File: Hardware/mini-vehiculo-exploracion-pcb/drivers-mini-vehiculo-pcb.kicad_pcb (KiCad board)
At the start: 2 copper layers, 75.5 x 100 mm, 56 parts, among them IC1 MAX8891EXK33_V+T, J1 Conn_01x08_Pin_drv, J2 Conn_01x02_Pin_drv, J4 Motor1_Terminal, J5 Motor2_Terminal, J6 Battery_Terminal_01x02, U1 DRV8873HPWPRQ1, U2 DRV8873HPWPRQ1, U3 TPS561208DDCR, U4 LM358

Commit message: cambios rama de drivers
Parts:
- L1: value 4,7u -> MLP2520S4R7MT0S1
- moved L1 1.00 mm to (74.0, 116.5)
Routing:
- net +5V: track 16.4 -> 21.9 mm
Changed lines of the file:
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@@
 		)
 	)
-	(footprint "MLP2520S4R7MT0S1:INDC2520X100N"
-		(layer "F.Cu")
-		(at 73.9 115.5)
-		(descr "MLP2520")
-		(tags "Inductor")
-		(property "Reference" "L1"
-			(at -0.06 2.28 0)
-			(layer "F.SilkS")
-			(effects
-				(font
-					(size 1.27 1.27)
-					(thickness 0.254)
-				)
-			)
-		)
-		(property "Value" "4,7u"
-			(at 0 0 0)
-			(layer "F.SilkS")
-			(hide yes)
-			(effects
-				(font
-					(size 1.27 1.27)
-					(thickness 0.254)
-				)
-			)
-		)
-		(property "Datasheet" "~"
-			(at 0 0 0)
-			(layer "F.Fab")
-			(hide yes)
-			(effects
-				(font
-					(size 1.27 1.27)
-					(thickness 0.15)
-				)
-			)
-		)
-		(property "Description" "Inductor"
-			(at 0 0 0)
-			(layer "F.Fab")
-			(hide yes)
-			(effects
-				(font
-					(size 1.27 1.27)
-					(thickness 0.15)
-				)
-			)
-		)
-		(property ki_fp_filters "Choke_* *Coil* Inductor_* L_*")
-		(sheetname "/Electrical/")
-		(sheetfile "electrical_drivers.kicad_sch")
-		(attr smd)
-		(fp_line
-			(start 0 -0.9)
-			(end 0 0.9)
-			(stroke
-				(width 0.2)
-				(type solid)
-			)
-			(layer "F.SilkS")
-		)
-		(fp_line
-			(start -1.925 -1.35)
-			(end 1.925 -1.35)
-			(stroke
-				(width 0.05)
-				(type solid)
-			)
-			(layer "F.CrtYd")
-		)
-		(fp_line
-			(start -1.925 1.35)
-			(end -1.925 -1.35)
-			(stroke
-				(width 0.05)
-				(type solid)
-			)
-			(layer "F.CrtYd")
-		)
-		(fp_line
-			(start 1.925 -1.35)
-			(end 1.925 1.35)
-			(stroke
-				(width 0.05)
-				(type solid)
-			)
-			(layer "F.CrtYd")
-		)
-		(fp_line
-			(start 1.925 1.35)
-			(end -1.925 1.35)
-			(stroke
-				(width 0.05)
-				(type solid)
-			)
-			(layer "F.CrtYd")
-		)
-		(fp_line
-			(start -1.25 -1)
-			(end 1.25 -1)
-			(stroke
-				(width 0.1)
-				(type solid)
-			)
-			(layer "F.Fab")
-		)
-		(fp_line
-			(start -1.25 1)
-			(end -1.25 -1)
-			(stroke
-				(width 0.1)
-				(type solid)
-			)
-			(layer "F.Fab")
-		)
-		(fp_line
-			(start 1.25 -1)
-			(end 1.25 1)
-			(stroke
-				(width 0.1)
-				(type solid)
-			)
-			(layer "F.Fab")
-		)
-		(fp_line
-			(start 1.25 1)
-			(end -1.25 1)
-			(stroke
-				(width 0.1)
-				(type solid)
-			)
-			(layer "F.Fab")
-		)
-		(pad "1" smd rect
-			(at -1.1 0)
-			(size 1.15 2.2)
-			(layers "F.Cu" "F.Mask" "F.Paste")
-			(net 25 "Net-(U3-SW)")
-			(pinfunction "1")
-			(pintype "passive")
-		)
-		(pad "2" smd rect
-			(at 1.1 0)
-			(size 1.15 2.2)
-			(layers "F.Cu" "F.Mask" "F.Paste")
-			(net 5 "+5V")
-			(pinfunction "2")
-			(pintype "passive")
-		)
-		(embedded_fonts no)
-		(model "MLP2520S4R7MT0S1.stp"
-			(offset
-				(xyz 0 0 0)
-			)
-			(scale
-				(xyz 1 1 1)
-			)
-			(rotate
-				(xyz 0 0 0)
-			)
-		)
-	)
 	(footprint "Capacitor_SMD:C_0805_2012Metric_Pad1.18x1.45mm_HandSolder"
 		(layer "F.Cu")
@@
 		)
 	)
+	(footprint "MLP2520S4R7MT0S1:INDC2520X100N"
+		(layer "F.Cu")
+		(at 74 116.5)
+		(descr "MLP2520")
+		(tags "Inductor")
+		(property "Reference" "L1"
+			(at 0 0 0)
+			(layer "F.SilkS")
+			(effects
+				(font
+					(size 1.27 1.27)
+					(thickness 0.254)
+				)
+			)
+		)
+		(property "Value" "MLP2520S4R7MT0S1"
+			(at 0 0 0)
+			(layer "F.SilkS")
+			(hide yes)
+			(effects
+				(font
+					(size 1.27 1.27)
+					(thickness 0.254)
+				)
+			)
+		)
+		(property "Datasheet" "https://product.tdk.com/system/files/dam/doc/product/inductor/inductor/smd/catalog/inductor_commercial_power_mlp2520_en.pdf"
+			(at 0 0 0)
+			(layer "F.Fab")
+			(hide yes)
+			(effects
+				(font
+					(size 1.27 1.27)
+					(thickness 0.15)
+				)
+			)
+		)
+		(property "Description" "Inductor Power Shielded Multi-Layer 4.7uH 20% 2MHz Ferrite 1A 169mOhm DCR 1008 T/R"
+			(at 0 0 0)
+			(layer "F.Fab")
+			(hide yes)
+			(effects
+				(font
+					(size 1.27 1.27)
+					(thickness 0.15)
+				)
+			)
+		)
+		(property "Height" "1"
+			(at 0 0 0)
+			(unlocked yes)
+			(layer "F.Fab")
+			(hide yes)
+			(effects
+				(font
+					(size 1 1)
+					(thickness 0.15)
+				)
+			)
+		)
+		(property "Mouser Part Number" "810-MLP2520S4R7MT0S1"
+			(at 0 0 0)
+			(unlocked yes)
+			(layer "F.Fab")
+			(hide yes)
+			(effects
+				(font
+					(size 1 1)
+					(thickness 0.15)
+				)
+			)
+		)
+		(property "Mouser Price/Stock" "https://www.mouser.co.uk/ProductDetail/TDK/MLP2520S4R7MT0S1?qs=%2FPzWLGNeQ%252BgDk3obJem54g%3D%3D"
+			(at 0 0 0)
+			(unlocked yes)
+			(layer "F.Fab")
+			(hide yes)
+			(effects
+				(font
+					(size 1 1)
+					(thickness 0.15)
+				)
+			)
+		)
+		(property "Manufacturer_Name" "TDK"
+			(at 0 0 0)
+			(unlocked yes)
+			(layer "F.Fab")
+			(hide yes)
+			(effects
+				(font
+					(size 1 1)
+					(thickness 0.15)
+				)
+			)
+		)
+		(property "Manufacturer_Part_Number" "MLP2520S4R7MT0S1"
+			(at 0 0 0)
+			(unlocked yes)
+			(layer "F.Fab")
+			(hide yes)
+			(effects
+				(font
+					(size 1 1)
+					(thickness 0.15)
+				)
+			)
+		)
+		(sheetname "/Electrical/")
+		(sheetfile "electrical_drivers.kicad_sch")
+		(attr smd)
+		(fp_line
+			(start 0 -0.9)
+			(end 0 0.9)
+			(stroke
+				(width 0.2)
+				(type solid)
+			)
+			(layer "F.SilkS")
+		)
+		(fp_line
+			(start -1.925 -1.35)
+			(end 1.925 -1.35)
+			(stroke
+				(width 0.05)
+				(type solid)
+			)
+			(layer "F.CrtYd")
+		)
+		(fp_line
+			(start -1.925 1.35)
+			(end -1.925 -1.35)
+			(stroke
+				(width 0.05)
+				(type solid)
+			)
+			(layer "F.CrtYd")
+		)
+		(fp_line
+			(start 1.925 -1.35)
+			(end 1.925 1.35)
+			(stroke
+				(width 0.05)
+				(type solid)
+			)
+			(layer "F.CrtYd")
+		)
+		(fp_line
+			(start 1.925 1.35)
+			(end -1.925 1.35)
+			(stroke
+				(width 0.05)
+				(type solid)
+			)
+			(layer "F.CrtYd")
+		)
+		(fp_line
+			(start -1.25 -1)
+			(end 1.25 -1)
+			(stroke
+				(width 0.1)
+				(type solid)
+			)
+			(layer "F.Fab")
+		)
+		(fp_line
+			(start -1.25 1)
+			(end -1.25 -1)
+			(stroke
+				(width 0.1)
+				(type solid)
+			)
+			(layer "F.Fab")
+		)
+		(fp_line
+			(start 1.25 -1)
+			(end 1.25 1)
+			(stroke
+				(width 0.1)
+				(type solid)
+			)
+			(layer "F.Fab")
+		)
+		(fp_line
+			(start 1.25 1)
+			(end -1.25 1)
+			(stroke
+				(width 0.1)
+				(type solid)
+			)
+			(layer "F.Fab")
+		)
+		(fp_text user "${REFERENCE}"
+			(at 0 0 0)
+			(layer "F.Fab")
+			(effects
+				(font
+					(size 1.27 1.27)
+					(thickness 0.254)
+				)
+			)
+		)
+		(pad "1" smd rect
+			(at -1.1 0)
+			(size 1.15 2.2)
+			(layers "F.Cu" "F.Mask" "F.Paste")
+			(net 25 "Net-(U3-SW)")
+			(pinfunction "1")
+			(pintype "passive")
+		)
+		(pad "2" smd rect
+			(at 1.1 0)
+			(size 1.15 2.2)
+			(layers "F.Cu" "F.Mask" "F.Paste")
+			(net 5 "+5V")
+			(pinfunction "2")
+			(pintype "passive")
+		)
+		(embedded_fonts no)
+		(model "MLP2520S4R7MT0S1.stp"
+			(offset
+				(xyz 0 0 0)
+			)
+			(scale
+				(xyz 1 1 1)
+			)
+			(rotate
+				(xyz 0 0 0)
+			)
+		)
+	)
 	(footprint "LM358AN_NOPB:DIP794W53P254L959H508Q8N"
 		(layer "F.Cu")
@@
 		(start 69.415 102.125)
 		(end 62.99 102.125)
-		(width 0.4)
+		(width 1.2)
 		(layer "F.Cu")
 		(net 2)
@@
 		(start 53.885 101.04)
 		(end 60.305 101.04)
-		(width 0.4)
+		(width 1.2)
 		(layer "F.Cu")
 		(net 2)
@@
 		(start 62.99 102.125)
 		(end 62.09 101.225)
-		(width 0.4)
+		(width 1.2)
 		(layer "F.Cu")
 		(net 2)
@@
 		(start 62.09 101.225)
 		(end 60.49 101.225)
-		(width 0.4)
+		(width 1.2)
 		(layer "F.Cu")
 		(net 2)
@@
 		(layer "F.Cu")
 		(net 5)
+	)
+	(segment
+		(start 76.949 116.5)
+		(end 79.499 119.05)
+		(width 0.4)
+		(layer "F.Cu")
+		(net 5)
+	)
+	(segment
+		(start 75.1 116.5)
+		(end 76.949 116.5)
+		(width 0.4)
+		(layer "F.Cu")
+		(net 5)

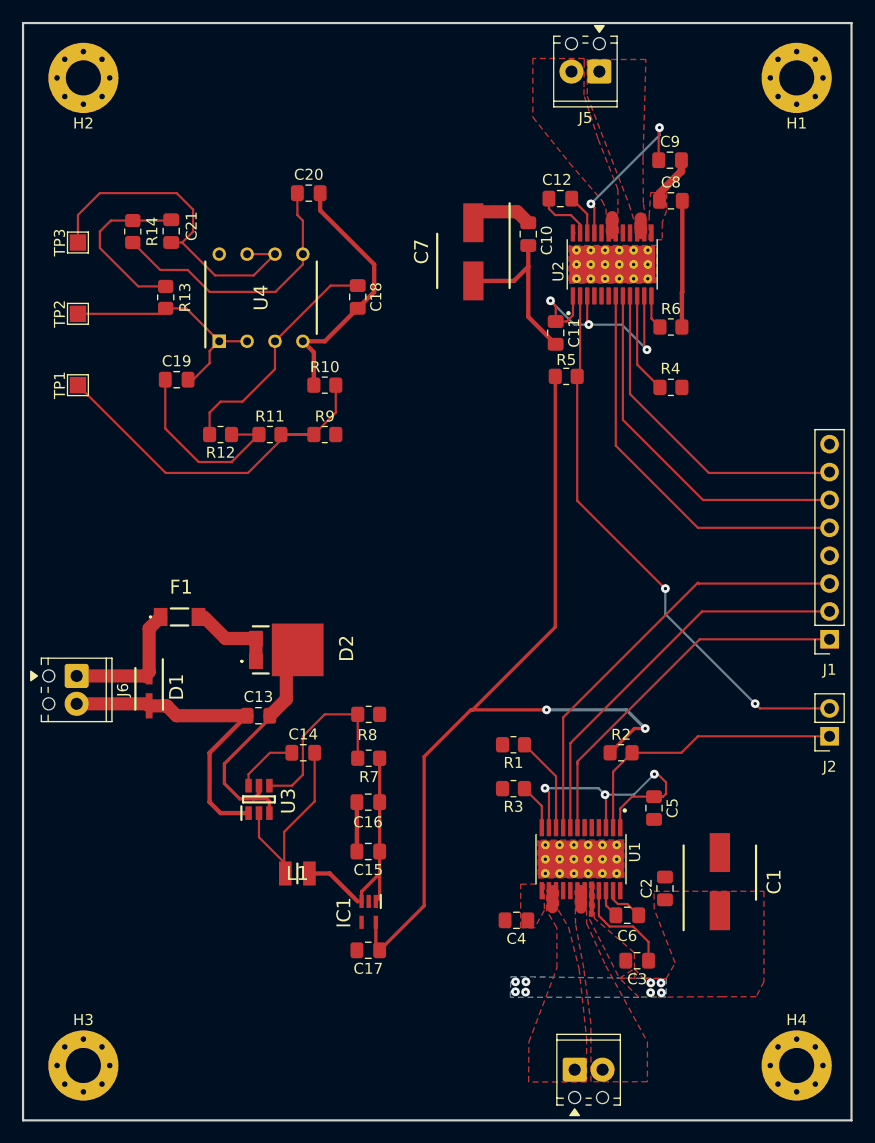
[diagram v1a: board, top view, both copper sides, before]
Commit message: updated gnd and 12v zones
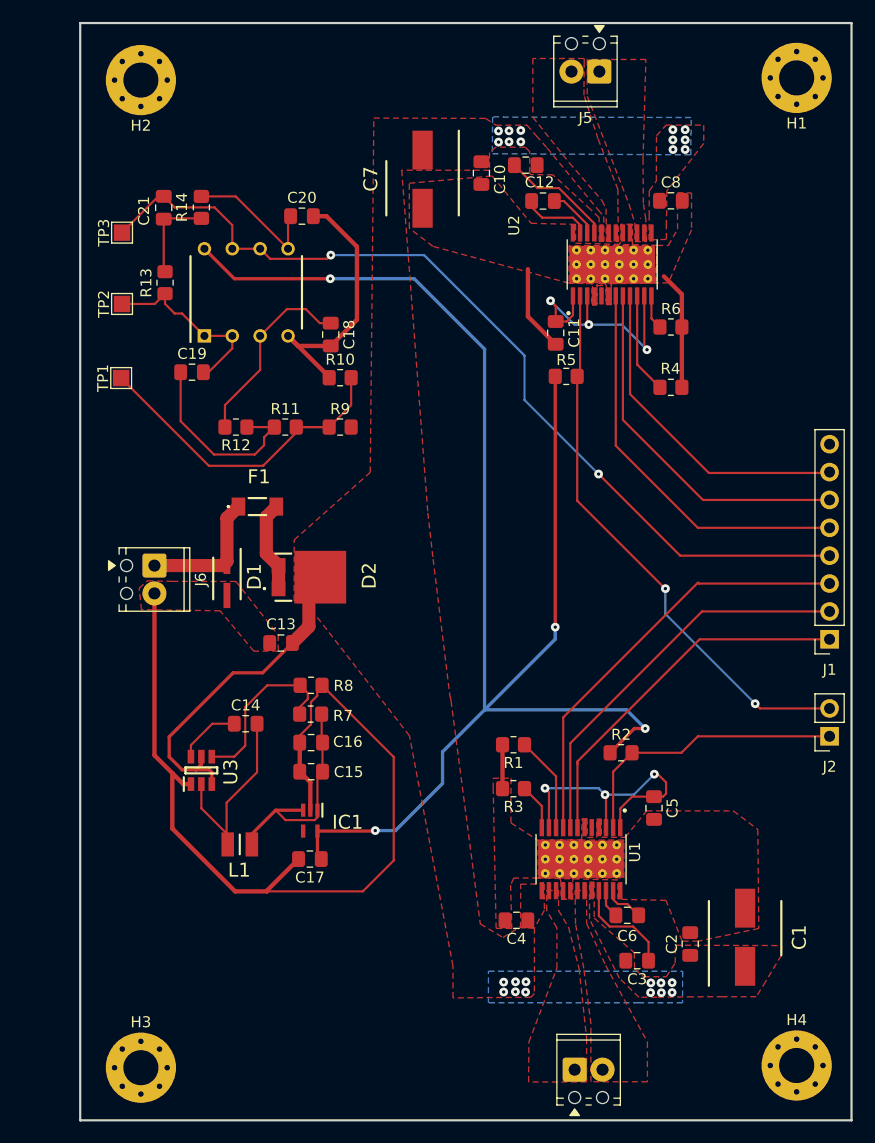
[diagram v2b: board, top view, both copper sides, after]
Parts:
- moved C9 13.2 mm to (94.8, 52.0)
- moved F1 12.3 mm to (70.4, 83.1)
- moved J6 12.3 mm to (61.0, 88.4)
- moved D1 12.3 mm to (67.6, 89.6)
- moved C17 9.87 mm to (75.1, 115.2)
- moved IC1 9.87 mm to (75.2, 111.7)
- moved C15 8.95 mm to (75.3, 107.2)
- moved C7 8.08 mm to (85.4, 53.2)
- moved C16 7.52 mm to (75.3, 104.6)
- moved C10 7.01 mm to (90.8, 52.7)
- moved C13 6.94 mm to (72.5, 95.5)
- moved D2 6.94 mm to (75.0, 89.5)
- moved R7 6.65 mm to (75.2, 102.0)
- moved R14 6.63 mm to (65.2, 55.8), turned to 90 degrees
- moved C14 5.88 mm to (69.3, 102.9)
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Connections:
- J1 pad 4: unconnected-(J1-Pin_4-Pad4) -> ADC_BAT
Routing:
- net +3.3V: track 82.4 -> 138.9 mm, vias 2 -> 4
- net ADC_BAT: track 32.3 -> 83.7 mm, vias 0 -> 2
- net GND: track 84.7 -> 130.9 mm
- net Net-(U4B-+): track 25.1 -> 12.9 mm
- net Net-(C21-Pad1): track 15.9 -> 8.40 mm
- net /VCP2: track 15.3 -> 10.4 mm, vias 2 -> 0
- net /Battery Sensor/OP1_OUT: track 21.8 -> 17.3 mm
- net Net-(U4A-+): track 21.8 -> 17.6 mm
- net +12V: track 34.8 -> 30.8 mm, vias 8 -> 24
- net Net-(R10-Pad2): track 34.6 -> 32.1 mm
- net /M1_V+: track 2.23 -> 0.00 mm
- net /M1_V-: track 2.29 -> 0.11 mm
- net /M2_V+: track 2.13 -> 0.03 mm
- net /M2_V-: track 2.24 -> 0.26 mm
- net +5V: track 21.9 -> 20.6 mm
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- added copper zone on B.Cu, net GND
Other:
- board size 75.5 x 100 mm -> 70.3 x 100 mm

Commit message: updated gnd plane
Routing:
- net GND: track 130.9 -> 1.36 mm

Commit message: updated driver pcb
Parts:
- moved J1 1.38 mm to (121.1, 95.2)
- moved J2 1.38 mm to (121.1, 104.0)
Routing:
- net /M2_DISABLE: track 30.1 -> 28.7 mm
- net /M2_IN1: track 36.2 -> 34.9 mm
- net /M1_IN2: track 36.3 -> 34.9 mm
- net /M1_IN1: track 33.6 -> 32.3 mm
- net /M1_nFAULT: track 26.2 -> 24.8 mm
- net /M1_DISABLE: track 39.4 -> 38.1 mm
- net ADC_BAT: track 83.7 -> 82.3 mm
- net /M2_nFAULT: track 50.9 -> 49.6 mm
- net /M2_IN2: track 33.2 -> 31.8 mm
- net GND: vias 0 -> 322
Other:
- board size 70.3 x 100 mm -> 70.3 x 98.5 mm
- board text added: "C9"
